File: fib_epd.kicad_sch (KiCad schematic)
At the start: 54 parts, among them U1 TPS651851RSLT, U4 ESP32-S3-WROOM-1U

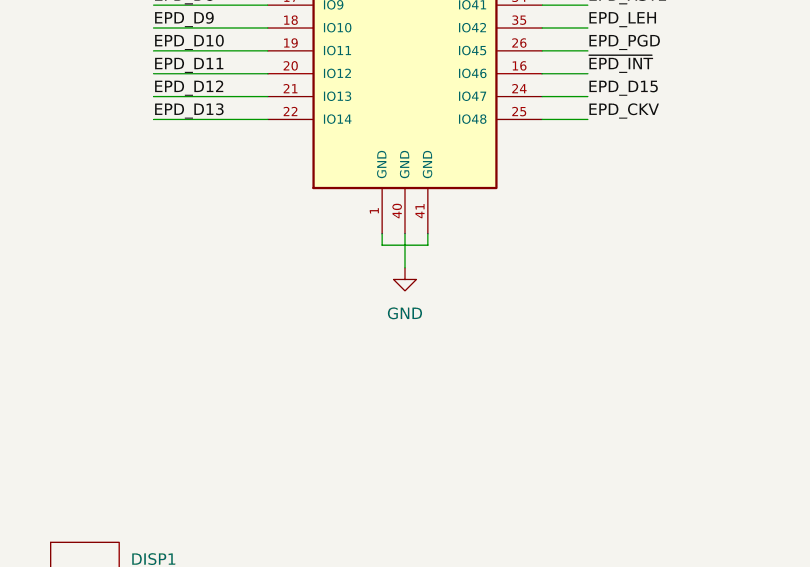
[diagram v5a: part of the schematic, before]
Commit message: 90 percent done with routing. need to go over all schematic pages, double check everything thoroughly, do lengthmatching add any missing footprints, take care of startup, ferrites, audio, eink connectors, 40pin header connections, rtc
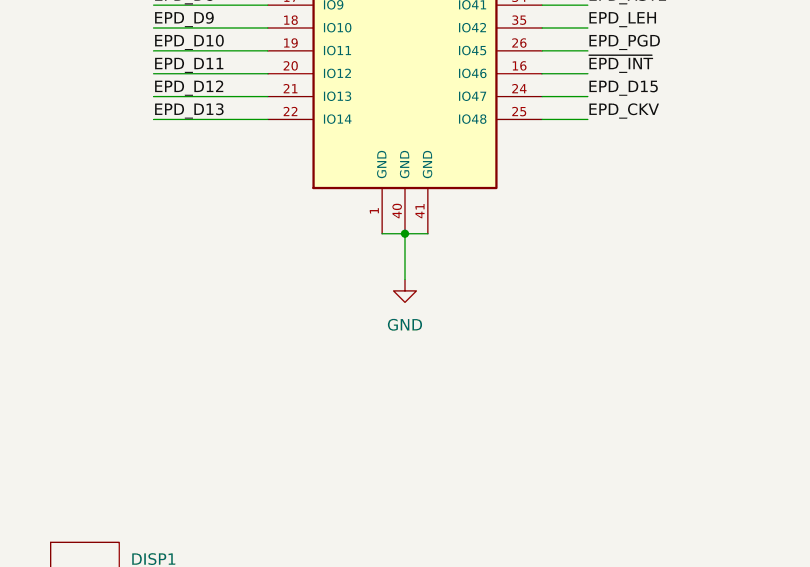
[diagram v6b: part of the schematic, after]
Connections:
- net GND: now also U4.1 (GND), U4.41 (GND)
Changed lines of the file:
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@@
 	)
 	(junction
+		(at 228.6 95.25)
+		(diameter 0)
+		(color 0 0 0 0)
+	)
+	(junction
 		(at 50.8 104.14)
 		(diameter 0)
@@
 	(wire
 		(pts
-			(xy 226.06 96.52) (xy 231.14 96.52)
-		)
-		(stroke
-			(width 0)
-			(type default)
-		)
-	)
-	(wire
-		(pts
 			(xy 135.89 27.94) (xy 135.89 36.83)
 		)
@@
 	(wire
 		(pts
+			(xy 228.6 95.25) (xy 226.06 95.25)
+		)
+		(stroke
+			(width 0)
+			(type default)
+		)
+	)
+	(wire
+		(pts
 			(xy 48.26 33.02) (xy 48.26 34.29)
 		)
@@
 	(wire
 		(pts
-			(xy 226.06 96.52) (xy 226.06 95.25)
-		)
-		(stroke
-			(width 0)
-			(type default)
-		)
-	)
-	(wire
-		(pts
 			(xy 243.84 46.99) (xy 259.08 46.99)
 		)
@@
 	(wire
 		(pts
-			(xy 231.14 96.52) (xy 231.14 95.25)
+			(xy 26.67 62.23) (xy 26.67 69.85)
 		)
 		(stroke
@@
 	(wire
 		(pts
-			(xy 26.67 62.23) (xy 26.67 69.85)
+			(xy 52.07 175.26) (xy 40.64 175.26)
 		)
 		(stroke
@@
 	(wire
 		(pts
-			(xy 52.07 175.26) (xy 40.64 175.26)
+			(xy 25.4 175.26) (xy 25.4 177.8)
 		)
 		(stroke
@@
 	(wire
 		(pts
-			(xy 25.4 175.26) (xy 25.4 177.8)
+			(xy 33.02 186.69) (xy 40.64 186.69)
 		)
 		(stroke
@@
 	(wire
 		(pts
-			(xy 33.02 186.69) (xy 40.64 186.69)
+			(xy 228.6 95.25) (xy 231.14 95.25)
 		)
 		(stroke
@@
 	(wire
 		(pts
-			(xy 228.6 95.25) (xy 228.6 99.06)
+			(xy 228.6 95.25) (xy 228.6 100.33)
 		)
 		(stroke
@@
 	(symbol
 		(lib_id "power:GND")
-		(at 228.6 99.06 0)
+		(at 228.6 100.33 0)
 		(unit 1)
 		(exclude_from_sim no)
@@
 		(fields_autoplaced yes)
 		(property "Reference" "#PWR01112"
-			(at 228.6 105.41 0)
+			(at 228.6 106.68 0)
 			(effects
 				(font
@@
 		)
 		(property "Value" "GND"
-			(at 228.6 104.14 0)
+			(at 228.6 105.41 0)
 			(effects
 				(font
@@
 		)
 		(property "Footprint" ""
-			(at 228.6 99.06 0)
+			(at 228.6 100.33 0)
 			(effects
 				(font
@@
 		)
 		(property "Datasheet" ""
-			(at 228.6 99.06 0)
+			(at 228.6 100.33 0)
 			(effects
 				(font
@@
 		)
 		(property "Description" "Power symbol creates a global label with name \"GND\" , ground"
-			(at 228.6 99.06 0)
+			(at 228.6 100.33 0)
 			(effects
 				(font

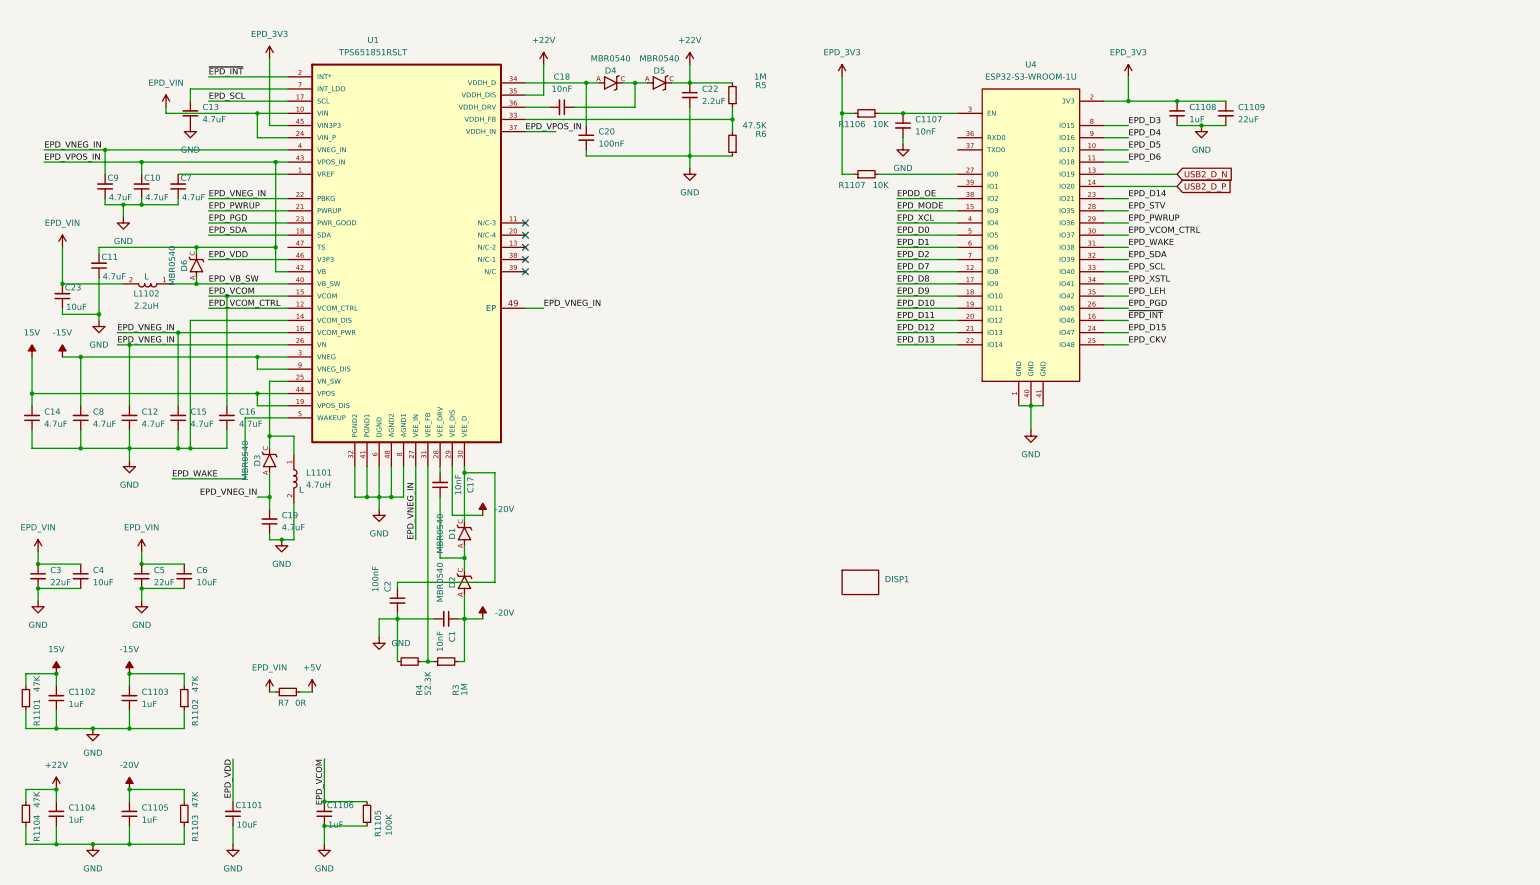
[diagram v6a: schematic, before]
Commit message: replaced 1v8 buck with ldo, added startup circuit, added footprints for eink connectors
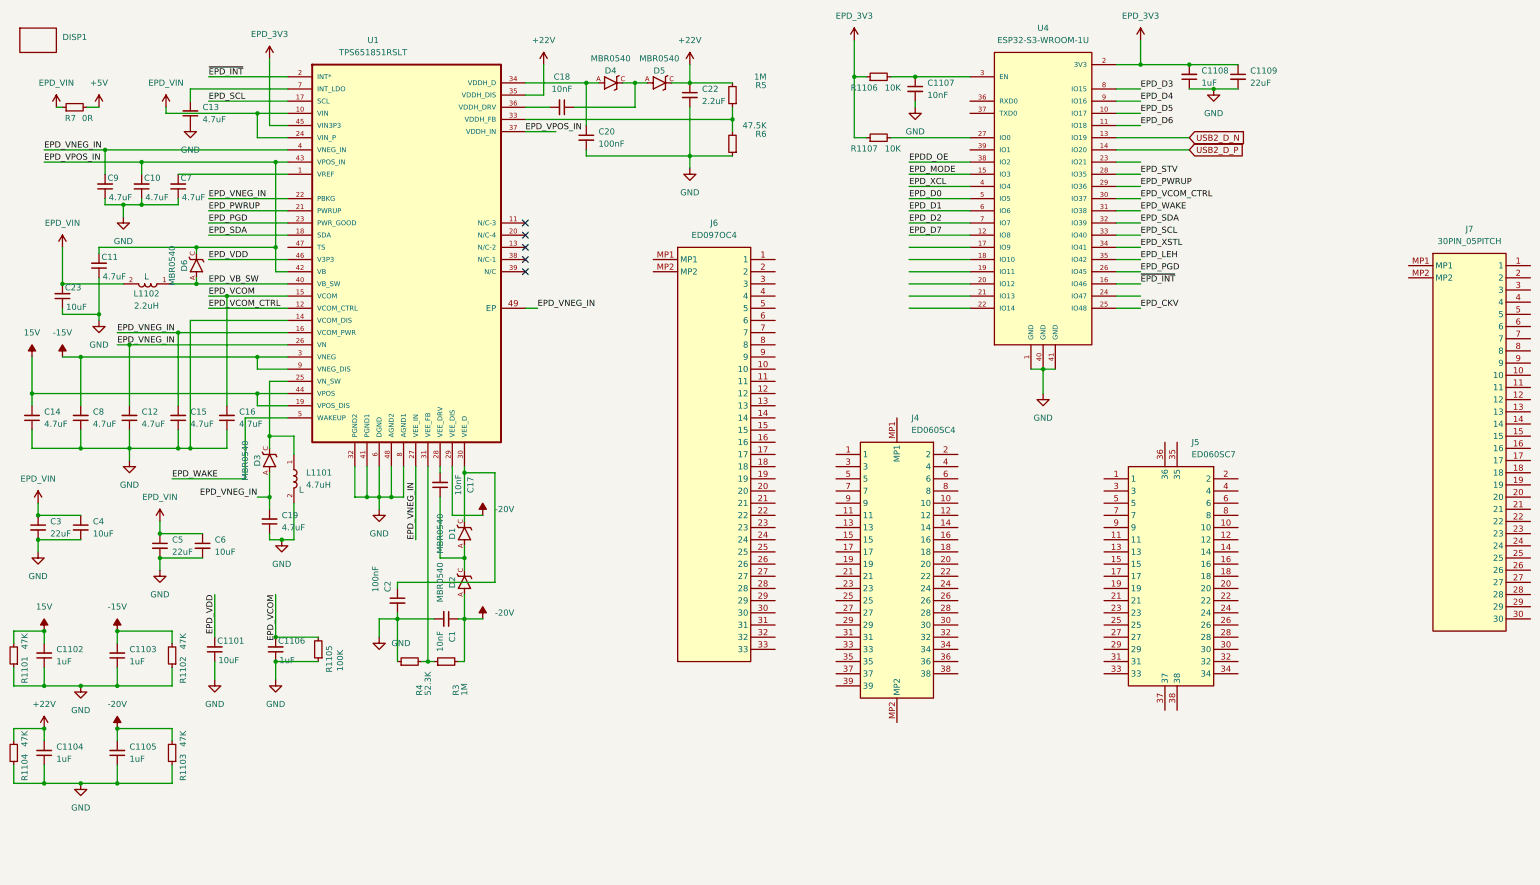
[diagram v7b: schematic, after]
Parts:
- added J4: ED060SC4, Fibel2:ED060SC4, symbol Fibel2:ED060SC4
- added J5: ED060SC7, Fibel2:ED060SC7, symbol Fibel2:ED060SC7
- added J6: ED097OC4, Fibel2:ED097OC4, symbol Fibel2:ED097OC4
- added J7: 30PIN_05PITCH, Fibel2:30PIN_05PITCH, symbol Fibel2:30PIN_05PITCH
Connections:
- net EPD_D10: no longer names the net of U4.19 (IO11)
- net EPD_D11: no longer names the net of U4.20 (IO12)
- net EPD_D12: no longer names the net of U4.21 (IO13)
- net EPD_D13: no longer names the net of U4.22 (IO14)
- net EPD_D14: no longer names the net of U4.23 (IO21)
- net EPD_D15: no longer names the net of U4.24 (IO47)
- net EPD_D8: no longer names the net of U4.17 (IO9)
- net EPD_D9: no longer names the net of U4.18 (IO10)
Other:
- moved on the sheet: C1101, C1102, C1103, C1104, C1105, C1106, C1107, C1108, C1109, C3, C4, C5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
